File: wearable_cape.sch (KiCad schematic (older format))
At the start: 80 parts, among them J1 JACK_3P, J2 JACK_3P, J3 JACK_3P, P1 BELA_AINS, P2 RECEIVER, P3 BATTERY, P4 BELA_AOUTS, P5 PWR_OUT, SW1 SW_HALT, SW2 SW_MODE_SEL, U1 MCP6004, U2 MCP6004, U3 BEAGLEBONEBLACK, U4 OKI_7805

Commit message: fixed minijack connections in schematic
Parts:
- added D1: RG_Led, symbol RG_Led
- added P6, P7: CONN_01X05, symbol CONN_01X05
- added R41: 560, symbol R
- added R42: 47, symbol R
- added SW3: SWITCH_SPDT, symbol SWITCH_SPDT
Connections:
- net D11: now also P6.2 (P2)
- net D8: now also P6.4 (P4)
- net D9: now also P6.5 (P5)
- net FILT_OUT0: now also J1.2 (T); no longer J1.3 (R)
- net FILT_OUT1: now also J3.2 (T); no longer J3.1 (S)
- net FILT_OUT2: now also J2.2 (T); no longer J2.3 (R)
- net FILT_OUT3: now also J2.3 (R); no longer J2.1 (S)
- net FILT_OUT5: now also J1.3 (R); no longer J1.1 (S)
- net GND: now also P6.3 (P3), P7.3 (P3), R42.1, SW3.3
- net GNDA: now also J1.1 (S), J2.1 (S), J3.1 (S); no longer J1.2 (T), J2.2 (T), J3.2 (T)
- net SYS_3.3V: now also P6.1 (P1)
- new net: R41.1, SW3.2
- new net: P7.2 (P2), R41.2
- new net: P7.1 (P1), SW3.1
- new net: D1.1 (GRN), P7.4 (P4)
- new net: D1.3 (RED), P7.5 (P5)
- new net: D1.2 (COM), R42.2
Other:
- note added: "Idle Switch & LED Board"
- moved on the sheet: C10, C12, C14, C15, C16, C17, C18, C19, C2, C20, C4, C7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

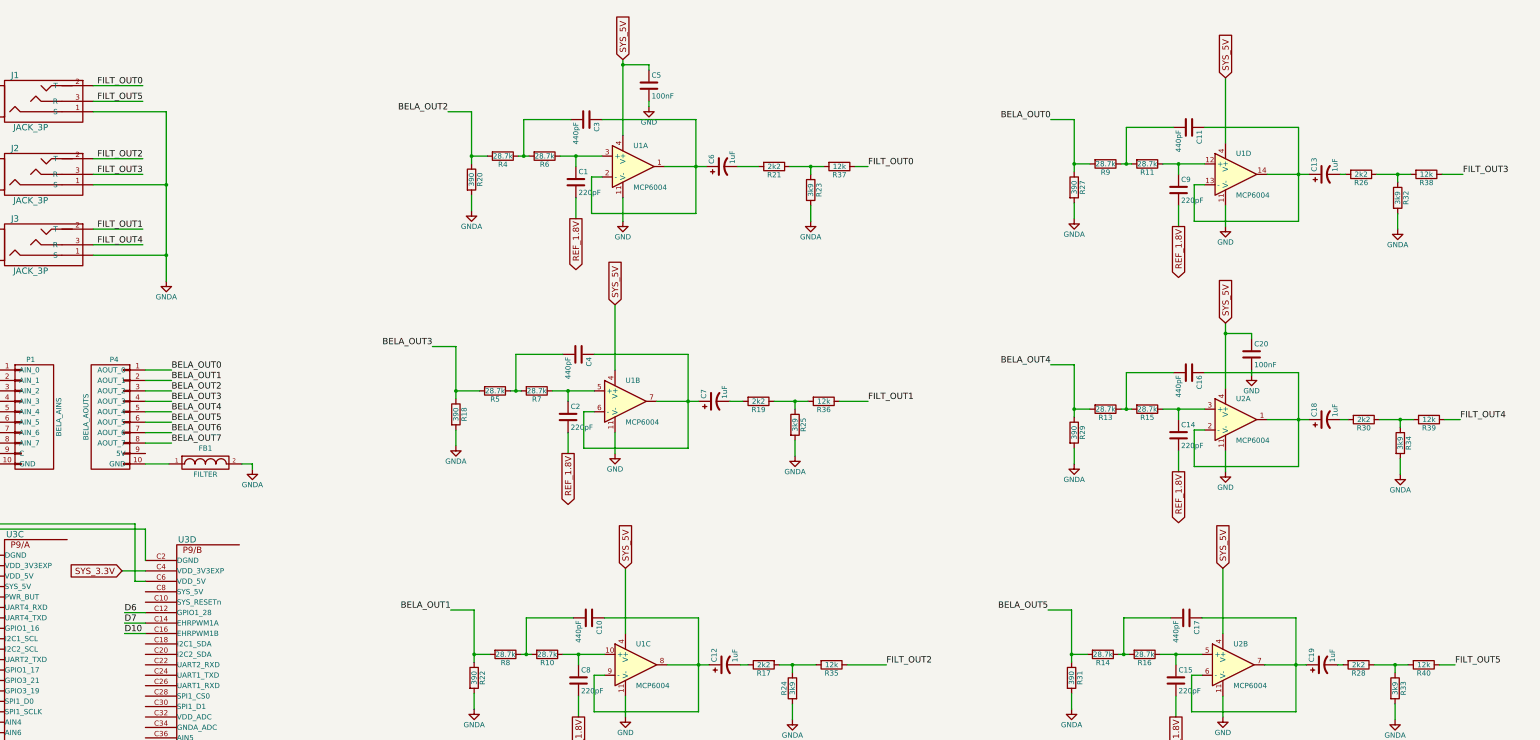
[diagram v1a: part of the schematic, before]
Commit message: fixed jack plugs pinout and made numbering of outputs consistent.
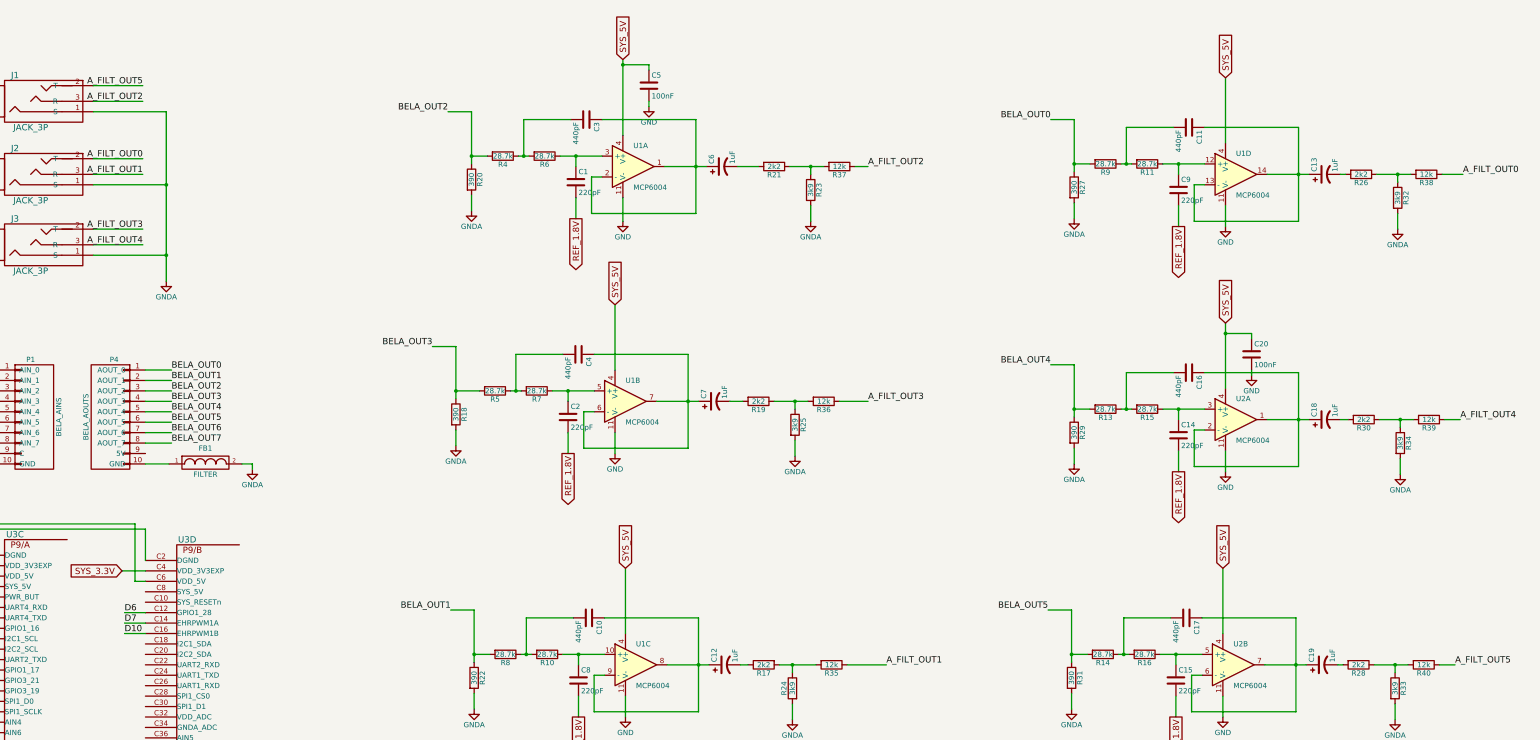
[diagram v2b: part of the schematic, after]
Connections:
- net FILT_OUT0 renamed A_FILT_OUT2
- net A_FILT_OUT2: now also J1.3 (R); no longer J1.2 (T)
- net FILT_OUT1 renamed A_FILT_OUT3
- net FILT_OUT2 renamed A_FILT_OUT0
- net A_FILT_OUT0: now also R38.1; no longer R35.1
- net FILT_OUT3 renamed A_FILT_OUT1
- net A_FILT_OUT1: now also R35.1; no longer R38.1
- net FILT_OUT4 renamed A_FILT_OUT4
- net FILT_OUT5 renamed A_FILT_OUT5
- net A_FILT_OUT5: now also J1.2 (T); no longer J1.3 (R)
